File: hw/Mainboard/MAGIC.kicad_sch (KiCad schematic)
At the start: 16 parts, among them U7 SN74LVC4245APWR, U8 SN74LVC4245APWR, U9 SN74LVC4245APWR

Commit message: hw: tidy
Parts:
- C31: value 1u -> 4.7u 10V; LCSC C52923 -> C23733
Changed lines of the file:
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@@
-    (pin "2")
-  )
-  (symbol (lib_id "Device:C_Small") (at 199.39 22.86 0) (unit 1)
-    (in_bom yes) (on_board yes)
-    (property "Reference" "C31" (id 0) (at 201.7268 21.6916 0)
-      (effects (font (size 1.27 1.27)) (justify left))
-    )
-    (property "Value" "1u" (id 1) (at 201.7268 24.003 0)
-      (effects (font (size 1.27 1.27)) (justify left))
-    )
-    (property "Footprint" "Capacitor_SMD:C_0402_1005Metric" (id 2) (at 199.39 22.86 0)
-      (effects (font (size 1.27 1.27)) hide)
-    )
-    (property "Datasheet" "https://datasheet.lcsc.com/lcsc/2304140030_Samsung-Electro-Mechanics-CL05A105KA5NQNC_C52923.pdf" (id 3) (at 199.39 22.86 0)
-      (effects (font (size 1.27 1.27)) hide)
-    )
-    (property "LCSC" "C52923" (id 4) (at 199.39 22.86 0)
-      (effects (font (size 1.27 1.27)) hide)
-    )
-    (pin "1")
     (pin "2")
   )
@@
       (effects (font (size 1.27 1.27)) hide)
     )
+    (pin "1")
+    (pin "2")
+  )
+  (symbol (lib_id "Device:C_Small") (at 199.39 22.86 0) (mirror y) (unit 1)
+    (in_bom yes) (on_board yes)
+    (property "Reference" "C31" (id 0) (at 197.0532 21.6916 0)
+      (effects (font (size 1.27 1.27)) (justify left))
+    )
+    (property "Value" "4.7u 10V" (id 1) (at 197.0532 24.003 0)
+      (effects (font (size 1.27 1.27)) (justify left))
+    )
+    (property "Footprint" "Capacitor_SMD:C_0402_1005Metric" (id 2) (at 199.39 22.86 0)
+      (effects (font (size 1.27 1.27)) hide)
+    )
+    (property "Datasheet" "https://datasheet.lcsc.com/lcsc/2304140030_Samsung-Electro-Mechanics-CL05A475MP5NRNC_C23733.pdf" (id 3) (at 199.39 22.86 0)
+      (effects (font (size 1.27 1.27)) hide)
+    )
+    (property "LCSC" "C23733" (id 4) (at 199.39 22.86 0)
+      (effects (font (size 1.27 1.27)) hide)
+    )

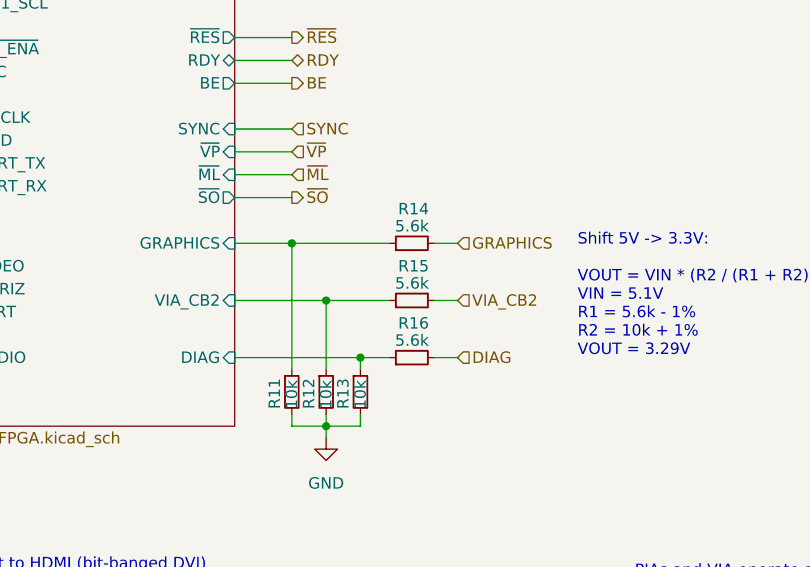
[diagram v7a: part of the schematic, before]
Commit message: hw: consistent resistor notation
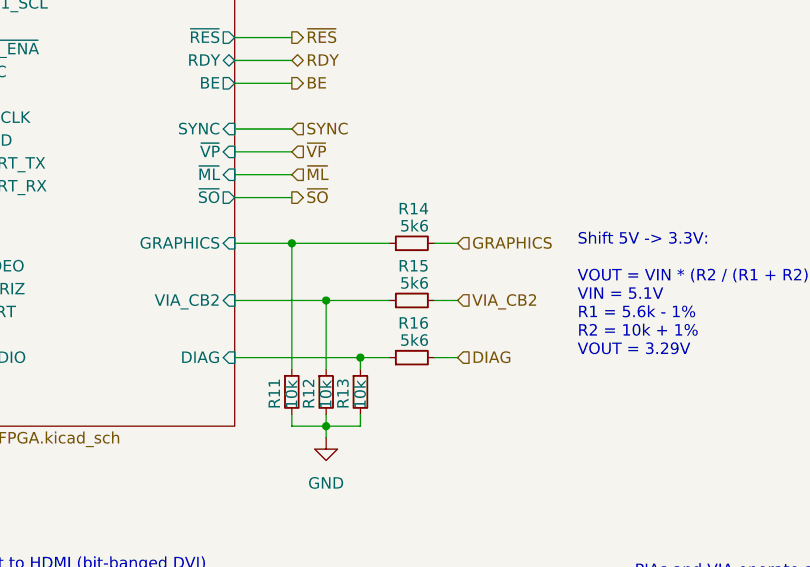
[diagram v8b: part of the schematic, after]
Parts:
- R14, R15, R16: value 5.6k -> 5k6
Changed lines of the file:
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@@
       (effects (font (size 1.27 1.27)) (justify left))
     )
-    (property "Value" "5.6k" (id 1) (at 104.14 114.935 90)
+    (property "Value" "5k6" (id 1) (at 104.14 114.935 90)
       (effects (font (size 1.27 1.27)) (justify left))
     )
@@
       (effects (font (size 1.27 1.27)) (justify left))
     )
-    (property "Value" "5.6k" (id 1) (at 104.14 108.585 90)
+    (property "Value" "5k6" (id 1) (at 104.14 108.585 90)
       (effects (font (size 1.27 1.27)) (justify left))
     )
@@
       (effects (font (size 1.27 1.27)) (justify left))
     )
-    (property "Value" "5.6k" (id 1) (at 104.14 102.235 90)
+    (property "Value" "5k6" (id 1) (at 104.14 102.235 90)
       (effects (font (size 1.27 1.27)) (justify left))
     )
